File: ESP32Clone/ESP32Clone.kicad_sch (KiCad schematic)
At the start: 47 parts, among them J1 Connector, USB-TYPE-C-16P, J2 Conn_01x08_Pin, J3 Conn_01x08_Pin, U1 TPS54331DR, U2 ESP32-C3FH4, U3 AHT20, U4 BH1750FVI-TR, U5 24LC1025-I_SM, X1 40MHz, 15pF

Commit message: Autosave and backup
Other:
- company: (none) -> Made by Adam Langeveld
- title: (none) -> ESP32 clone with I2C humidity, light sensor and eeprom
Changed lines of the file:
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@@
 	(generator_version "9.0")
 	(paper "A4")
+	(title_block
+		(title "ESP32 clone with I2C humidity, light sensor and eeprom")
+		(date "2026-01-01")
+		(rev "V1")
+		(company "Made by Adam Langeveld")
+		(comment 1 "Based around ESP32-C3FH4 microcontroller")
+		(comment 2 "USB-C power and data")
+	)
 	(rectangle
 		(start 82.55 102.87)
@@
 	)
 	(junction
+		(at 129.54 167.64)
+		(diameter 0)
+		(color 0 0 0 0)
+	)
+	(junction
 		(at 63.5 170.18)
 		(diameter 0)
@@
 	)
 	(junction
-		(at 144.78 52.07)
-		(diameter 0)
-		(color 0 0 0 0)
-	)
-	(junction
 		(at 53.34 34.29)
 		(diameter 0)
@@
 	(wire
 		(pts
-			(xy 153.67 52.07) (xy 144.78 52.07)
-		)
-		(stroke
-			(width 0)
-			(type default)
-		)
-	)
-	(wire
-		(pts
 			(xy 93.98 36.83) (xy 104.14 36.83)
 		)
@@
 	(wire
 		(pts
-			(xy 124.46 167.64) (xy 133.35 167.64)
+			(xy 124.46 167.64) (xy 129.54 167.64)
 		)
 		(stroke
@@
 	(wire
 		(pts
+			(xy 129.54 167.64) (xy 133.35 167.64)
+		)
+		(stroke
+			(width 0)
+			(type default)
+		)
+	)
+	(wire
+		(pts
 			(xy 38.1 74.93) (xy 40.64 74.93)
 		)
@@
 	(wire
 		(pts
-			(xy 144.78 52.07) (xy 128.27 52.07)
+			(xy 128.27 52.07) (xy 153.67 52.07)
 		)
 		(stroke
@@
 	)
 	(symbol
+		(lib_id "power:PWR_FLAG")
+		(at 129.54 167.64 0)
+		(unit 1)
+		(exclude_from_sim no)
+		(in_bom yes)
+		(on_board yes)
+		(dnp no)
+		(fields_autoplaced yes)
+		(property "Reference" "#FLG05"
+			(at 129.54 165.735 0)
+			(effects
+				(font
+					(size 1.27 1.27)
+				)
+				(hide yes)
+			)
+		)
+		(property "Value" "PWR_FLAG"
+			(at 129.54 162.56 0)
+			(effects
+				(font
+					(size 1.27 1.27)
+				)
+			)
+		)
+		(property "Footprint" ""
+			(at 129.54 167.64 0)
+			(effects
+				(font
+					(size 1.27 1.27)
+				)
+				(hide yes)
+			)
+		)
+		(property "Datasheet" "~"
+			(at 129.54 167.64 0)
+			(effects
+				(font
+					(size 1.27 1.27)
+				)
+				(hide yes)
+			)
+		)
+		(property "Description" "Special symbol for telling ERC where power comes from"
+			(at 129.54 167.64 0)
+			(effects
+				(font
+					(size 1.27 1.27)
+				)
+				(hide yes)
+			)
+		)
+		(pin "1"
+		)
+		(instances
+			(project ""
+				(path "/dd1e1a69-fb6d-4ec9-9346-c5821cbac777"
+					(reference "#FLG05")
+					(unit 1)
+				)
+			)
+		)
+	)
+	(symbol
 		(lib_id "24LC1025-I_SM:24LC1025-I_SM")
 		(at 205.74 39.37 0)
@@
 					(unit 1)
 				)
-			)
-		)
-	)
-	(symbol
-		(lib_id "power:PWR_FLAG")
-		(at 144.78 52.07 0)
-		(unit 1)
-		(exclude_from_sim no)
-		(in_bom yes)
-		(on_board yes)
-		(dnp no)
-		(fields_autoplaced yes)
-		(property "Reference" "#FLG07"
-			(at 144.78 50.165 0)
-			(effects
-				(font
-					(size 1.27 1.27)
-				)
-				(hide yes)
-			)
-		)
-		(property "Value" "PWR_FLAG"
-			(at 144.78 46.99 0)
-			(effects
-				(font
-					(size 1.27 1.27)
-				)
-			)
-		)
-		(property "Footprint" ""
-			(at 144.78 52.07 0)
-			(effects
-				(font
-					(size 1.27 1.27)
-				)
-				(hide yes)
-			)
-		)
-		(property "Datasheet" "~"
-			(at 144.78 52.07 0)
-			(effects
-				(font
-					(size 1.27 1.27)
-				)
-				(hide yes)
-			)
-		)
-		(property "Description" "Special symbol for telling ERC where power comes from"
-			(at 144.78 52.07 0)
-			(effects
-				(font
-					(size 1.27 1.27)
-				)
-				(hide yes)
-			)
-		)
-		(pin "1"
-		)
-		(instances
-			(project ""
-				(path "/dd1e1a69-fb6d-4ec9-9346-c5821cbac777"
-					(reference "#FLG07")
-					(unit 1)
-				)

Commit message: The thing i said before forgot to save
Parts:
- removed C14: 22uF, PCM_JLCPCB:C_0805, symbol PCM_JLCPCB-Capacitors:0805,22uF
- removed C15: 100uF, PCM_JLCPCB:C_1206, symbol PCM_JLCPCB-Capacitors:1206,100uF
- removed L2: 2.2uH,50mA, PCM_JLCPCB:L_0805, symbol PCM_JLCPCB-Inductors:2.2uH,50mA
- added C14: 1uF, PCM_JLCPCB:C_0603, symbol PCM_JLCPCB-Capacitors:0603,1uF
- added C15: 10uF, PCM_JLCPCB:C_0603, symbol PCM_JLCPCB-Capacitors:0603,10uF,(2)
- added C19: 4.7uF, PCM_JLCPCB:C_0805, symbol PCM_JLCPCB-Capacitors:0805,4.7uF
- added L2: 2.2mH, 50V, symbol Device:L
- added S2: Tactile Button, 160gf, PCM_JLCPCB:SW_TS-1088-AR02016, symbol PCM_JLCPCB-Connectors_Buttons:Tactile Button, 160gf, 12V, 50mA, 4.0mm
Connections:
- net GPIO 1 is gone; now on net GPIO 0: J2.3 (Pin_3), U2.5 (GPIO1/XTAL_32K_N)
- net 3.3V: now also J3.1 (Pin_1), L2.1; no longer J2.8 (Pin_8), J3.8 (Pin_8)
- net 5V: now also J2.8 (Pin_8); no longer J3.7 (Pin_7)
- net GND: now also C14.1, C15.1, C19.1; no longer J3.1 (Pin_1)
- net GPIO 0: now also U2.29 (XTAL_N), X1.3 (OSC), C15.2, C19.2
- net GPIO 2: now also S2.1 (A); no longer U2.6 (GPIO2)
- net at L3.1, X1.1 (OSC): now also C14.2
- net at C9.2, U2.2 (VDD3P3), U2.3 (VDD3P3): now also L2.2
- net GPIO 21: now reaches U2.27 (U0RXD)
- net GPIO 21: now also J3.8 (Pin_8)
- net GPIO 20: now reaches U2.28 (U0TXD)
- net GPIO 20: now also J3.7 (Pin_7)
- new net GPIO 2/IN: S2.2 (B), U2.6 (GPIO2)
- no-connect marks 14 -> 12
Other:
- note added: "Boot selector"
- moved on the sheet: R8, R9

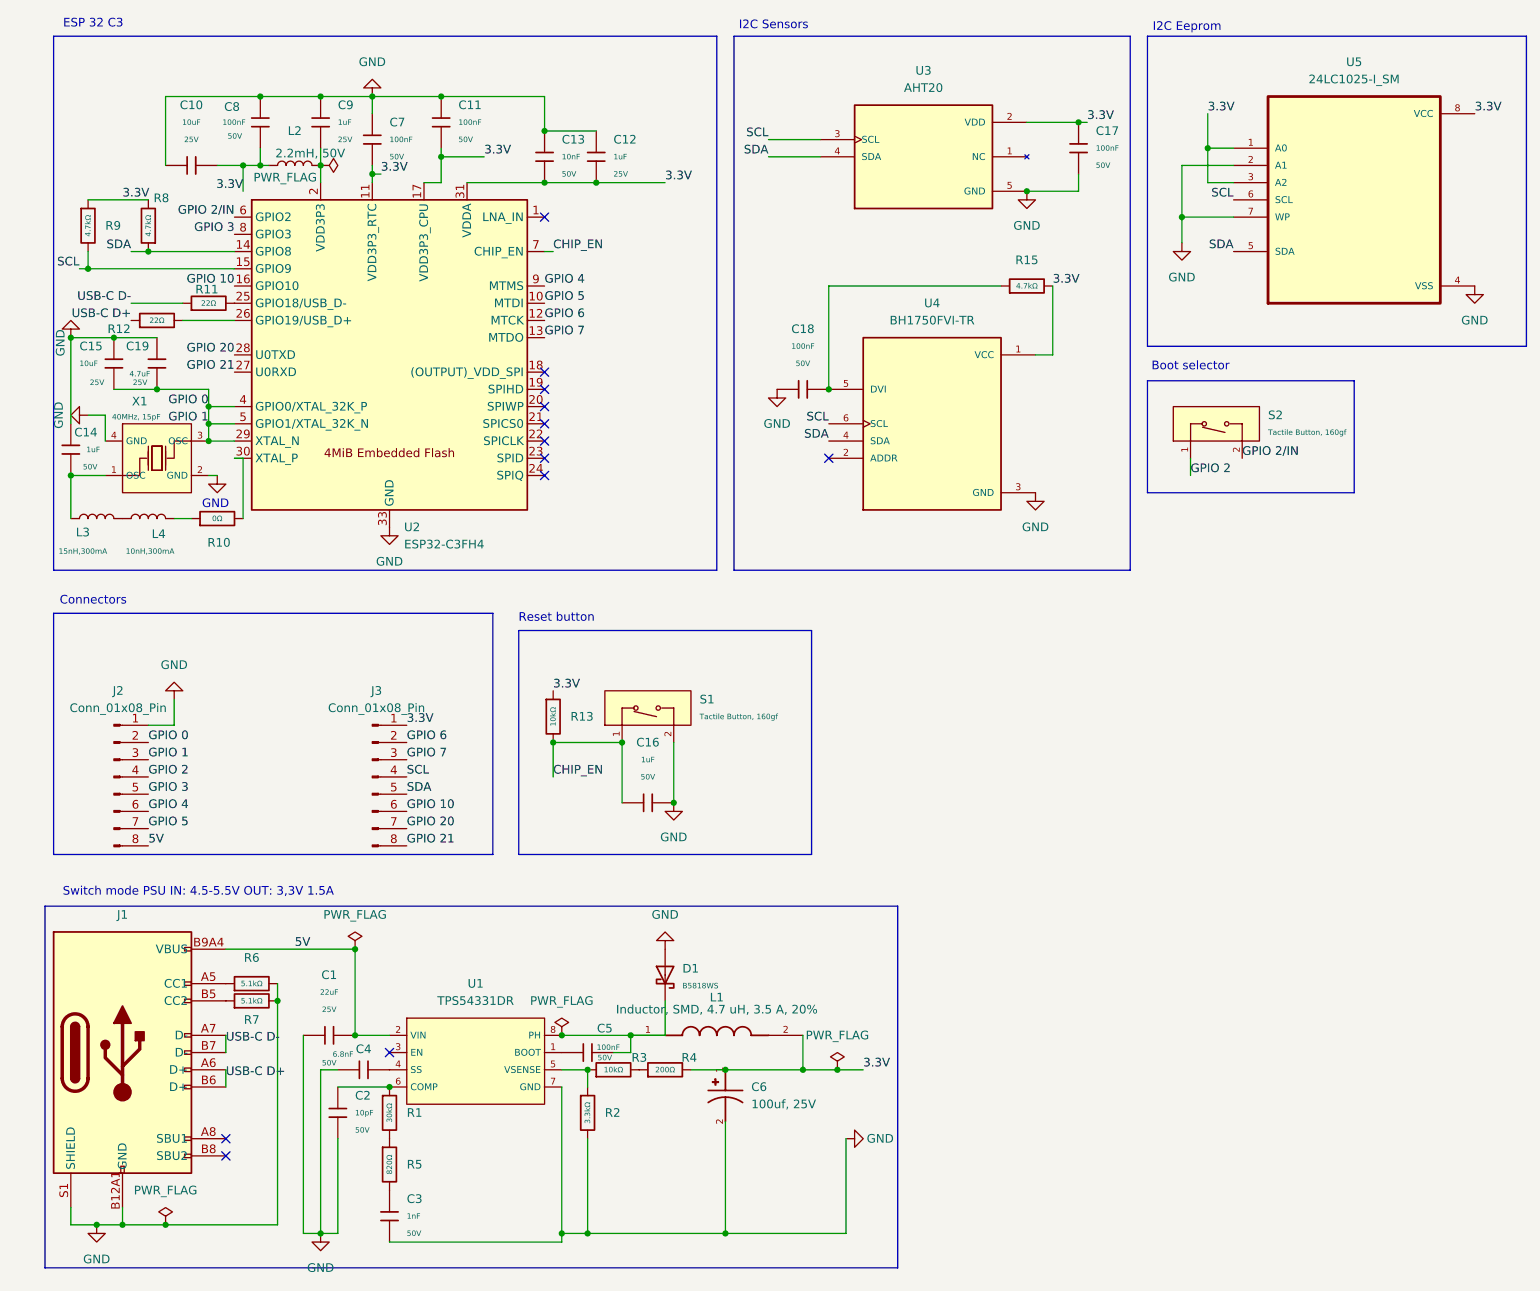
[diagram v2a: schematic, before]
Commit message: Fixed footprint
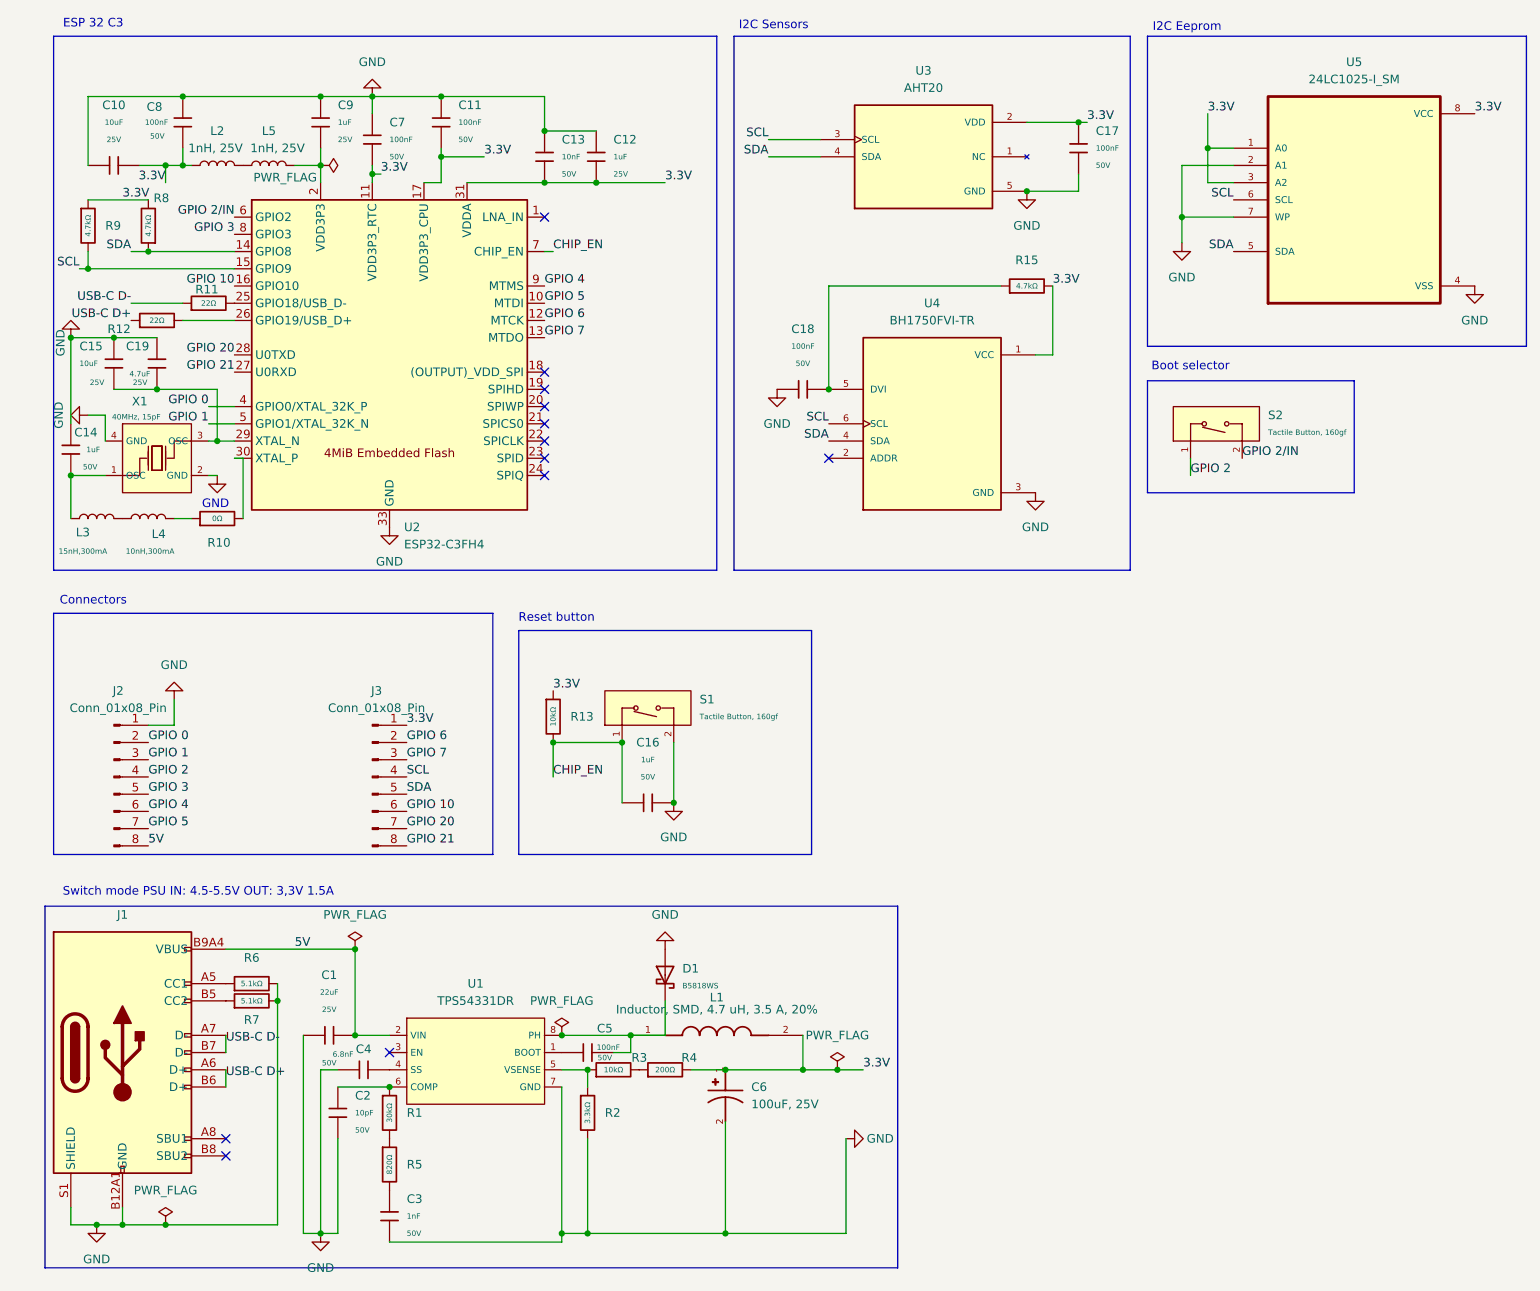
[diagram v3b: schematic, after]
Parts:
- added L5: 1nH, 25V, PCM_JLCPCB:L_0603, symbol Device:L
- C6: value 100uf, 25V -> 100uF, 25V; footprint JLCPCBExtended:CAPAE1050X1050N -> MAL214699103E3:CAPAE1050X1050N
- L2: value 2.2mH, 50V -> 1nH, 25V; footprint (none) -> PCM_JLCPCB:L_0603
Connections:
- net GPIO 0: no longer C15.2, C19.2, J2.3 (Pin_3), U2.29 (XTAL_N), U2.5 (GPIO1/XTAL_32K_N), X1.3 (OSC)
- net at C9.2, U2.2 (VDD3P3), U2.3 (VDD3P3): now also L5.2; no longer L2.2
- new net: C15.2, C19.2, U2.29 (XTAL_N), X1.3 (OSC)
- new net: L2.2, L5.1
- new net GPIO 1: J2.3 (Pin_3), U2.5 (GPIO1/XTAL_32K_N)
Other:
- moved on the sheet: C10, C8

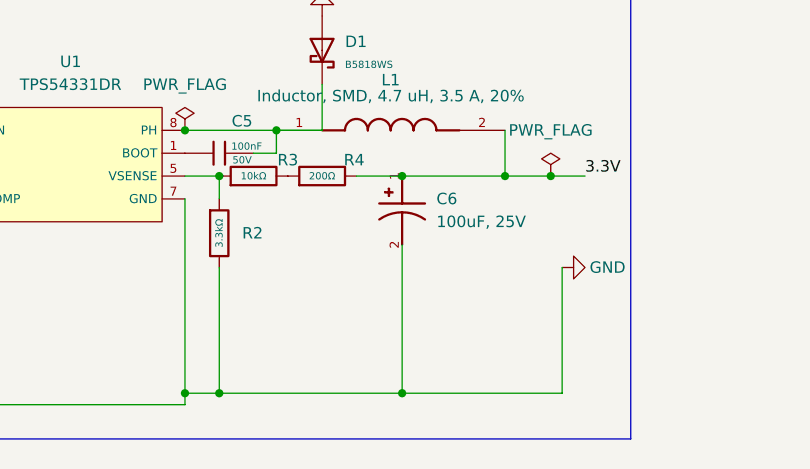
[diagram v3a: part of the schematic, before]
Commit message: Replaced capictor
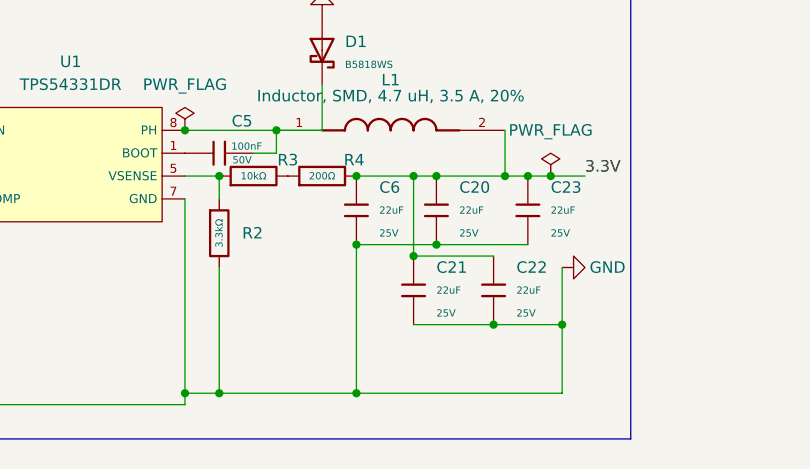
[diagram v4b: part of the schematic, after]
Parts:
- removed C6: 100uF, 25V, MAL214699103E3:CAPAE1050X1050N, symbol Capacitor-100uf-25V:MAL214699103E3
- added C20, C21, C22, C23, C6: 22uF, PCM_JLCPCB:C_0805, symbol PCM_JLCPCB-Capacitors:0805,22uF
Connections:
- net 3.3V: now also C20.1, C21.1, C22.1, C23.1, C6.1
- net GND: now also C20.2, C21.2, C22.2, C23.2, C6.2

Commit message: PCB started
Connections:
- net PRE3.3V: now reaches C5.1, D1.1, L1.1, U1.8 (PH)
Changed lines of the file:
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@@
+	)
+	(junction
+		(at 93.98 162.56)
+		(diameter 0)
+		(color 0 0 0 0)
 	)
 	(junction
@@
 	(wire
 		(pts
+			(xy 93.98 156.21) (xy 93.98 162.56)
+		)
+		(stroke
+			(width 0)
+			(type default)
+		)
+	)
+	(wire
+		(pts
 			(xy 53.34 31.75) (xy 53.34 34.29)
 		)
@@
 	(wire
 		(pts
-			(xy 99.06 162.56) (xy 88.9 162.56)
+			(xy 99.06 162.56) (xy 93.98 162.56)
 		)
 		(stroke
@@
 		(pts
 			(xy 97.79 119.38) (xy 97.79 128.27)
+		)
+		(stroke
+			(width 0)
+			(type default)
+		)
+	)
+	(wire
+		(pts
+			(xy 93.98 162.56) (xy 88.9 162.56)
 		)
 		(stroke
@@
 		)
 	)
+	(label "PRE3.3V"
+		(at 93.98 156.21 180)
+		(effects
+			(font
+				(size 1.27 1.27)
+			)
+			(justify right bottom)
+		)
+	)

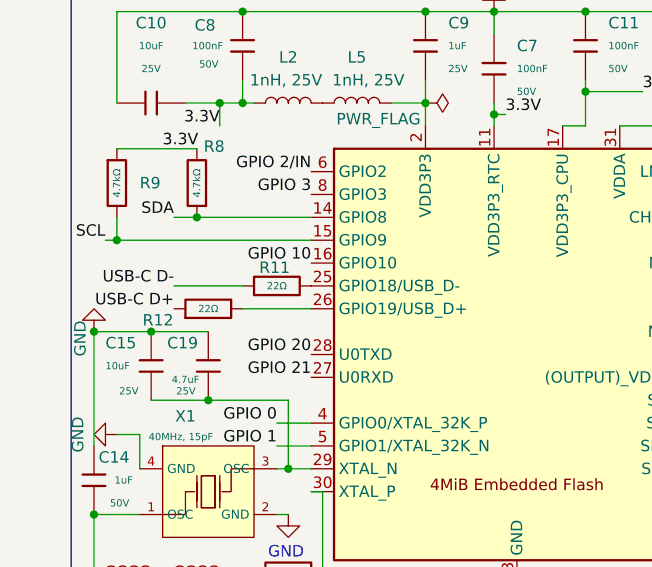
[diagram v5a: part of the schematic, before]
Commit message: Done DRC
only has a few library issue's left
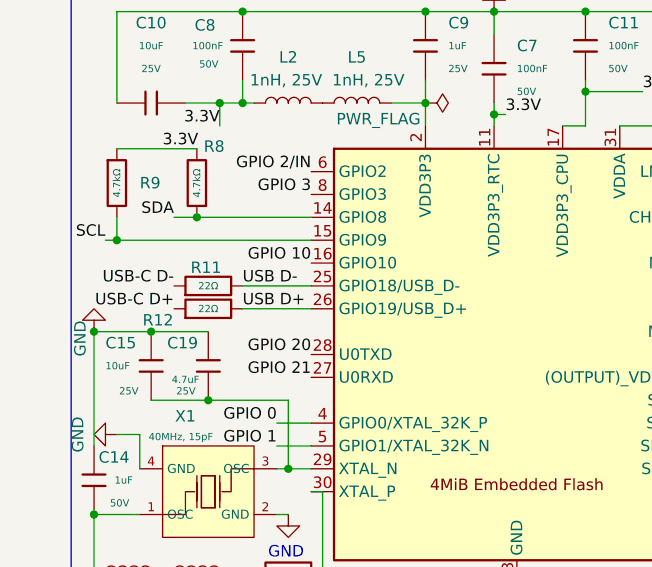
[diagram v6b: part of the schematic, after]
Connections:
- net USB D+: now reaches R12.2, U2.26 (GPIO19/USB_D+)
- net USB D-: now reaches R11.2, U2.25 (GPIO18/USB_D-)
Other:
- moved on the sheet: R11
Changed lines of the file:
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@@
 	(wire
 		(pts
+			(xy 33.02 54.61) (xy 40.64 54.61)
+		)
+		(stroke
+			(width 0)
+			(type default)
+		)
+	)
+	(wire
+		(pts
 			(xy 36.83 74.93) (xy 38.1 74.93)
 		)
@@
 	(wire
 		(pts
-			(xy 25.4 54.61) (xy 33.02 54.61)
-		)
-		(stroke
-			(width 0)
-			(type default)
-		)
-	)
-	(wire
-		(pts
 			(xy 16.51 80.01) (xy 16.51 86.36)
 		)
@@
 		)
 	)
+	(label "USB D+"
+		(at 33.02 57.15 0)
+		(effects
+			(font
+				(size 1.27 1.27)
+			)
+			(justify left bottom)
+		)
+	)
 	(label "GPIO 10"
 		(at 66.04 129.54 0)
@@
 		)
 	)
+	(label "USB D-"
+		(at 33.02 54.61 0)
+		(effects
+			(font
+				(size 1.27 1.27)
+			)
+			(justify left bottom)
+		)
+	)
 	(label "GPIO 2{slash}IN"
 		(at 189.23 77.47 0)
@@
 	(symbol
 		(lib_id "PCM_JLCPCB-Resistors:0805,22Ω")
-		(at 36.83 54.61 90)
+		(at 29.21 54.61 90)
 		(unit 1)
 		(exclude_from_sim no)
@@
 		(dnp no)
 		(property "Reference" "R11"
-			(at 36.576 52.578 90)
+			(at 28.956 52.578 90)
 			(effects
 				(font
@@
 		)
 		(property "Value" "22Ω"
-			(at 36.83 54.61 90)
+			(at 29.21 54.61 90)
 			(do_not_autoplace yes)
 			(effects
@@
 		)
 		(property "Footprint" "PCM_JLCPCB:R_0805"
-			(at 36.83 56.388 90)
+			(at 29.21 56.388 90)
 			(effects
 				(font
@@
 		)
 		(property "Datasheet" "https://www.lcsc.com/datasheet/lcsc_datasheet_2206010200_UNI-ROYAL-Uniroyal-Elec-0805W8F220JT5E_C17561.pdf"
-			(at 36.83 54.61 0)
+			(at 29.21 54.61 0)
 			(effects
 				(font
@@
 		)
 		(property "Description" "125mW Thick Film Resistors 150V ±100ppm/°C ±1% 22Ω 0805 Chip Resistor - Surface Mount ROHS"
-			(at 36.83 54.61 0)
+			(at 29.21 54.61 0)
 			(effects
 				(font
@@
 		)
 		(property "LCSC" "C17561"
-			(at 36.83 54.61 0)
+			(at 29.21 54.61 0)
 			(effects
 				(font
@@
 		)
 		(property "Stock" "551567"
-			(at 36.83 54.61 0)
+			(at 29.21 54.61 0)
 			(effects
 				(font
@@
 		)
 		(property "Price" "0.005USD"
-			(at 36.83 54.61 0)
+			(at 29.21 54.61 0)
 			(effects
 				(font
@@
 		)
 		(property "Process" "SMT"
-			(at 36.83 54.61 0)
+			(at 29.21 54.61 0)
 			(effects
 				(font
@@
 		)
 		(property "Minimum Qty" "20"
-			(at 36.83 54.61 0)
+			(at 29.21 54.61 0)
 			(effects
 				(font
@@
 		)
 		(property "Attrition Qty" "10"
-			(at 36.83 54.61 0)
+			(at 29.21 54.61 0)
 			(effects
 				(font
@@
 		)
 		(property "Class" "Basic Component"
-			(at 36.83 54.61 0)
+			(at 29.21 54.61 0)
 			(effects
 				(font
@@
 		)
 		(property "Category" "Resistors,Chip Resistor - Surface Mount"
-			(at 36.83 54.61 0)
+			(at 29.21 54.61 0)
 			(effects
 				(font
@@
 		)
 		(property "Manufacturer" "UNI-ROYAL(Uniroyal Elec)"
-			(at 36.83 54.61 0)
+			(at 29.21 54.61 0)
 			(effects
 				(font
@@
 		)
 		(property "Part" "0805W8F220JT5E"
-			(at 36.83 54.61 0)
+			(at 29.21 54.61 0)
 			(effects
 				(font
@@
 		)
 		(property "Resistance" "22Ω"
-			(at 36.83 54.61 0)
+			(at 29.21 54.61 0)
 			(effects
 				(font
@@
 		)
 		(property "Power(Watts)" "125mW"
-			(at 36.83 54.61 0)
+			(at 29.21 54.61 0)
 			(effects
 				(font
@@
 		)
 		(property "Type" "Thick Film Resistors"
-			(at 36.83 54.61 0)
+			(at 29.21 54.61 0)
 			(effects
 				(font
@@
 		)
 		(property "Overload Voltage (Max)" "150V"
-			(at 36.83 54.61 0)
+			(at 29.21 54.61 0)
 			(effects
 				(font
@@
 		)
 		(property "Operating Temperature Range" "-55°C~+155°C"
-			(at 36.83 54.61 0)
+			(at 29.21 54.61 0)
 			(effects
 				(font
@@
 		)
 		(property "Tolerance" "±1%"
-			(at 36.83 54.61 0)
+			(at 29.21 54.61 0)
 			(effects
 				(font
@@
 		)
 		(property "Temperature Coefficient" "±100ppm/°C"
-			(at 36.83 54.61 0)
+			(at 29.21 54.61 0)
 			(effects
 				(font
